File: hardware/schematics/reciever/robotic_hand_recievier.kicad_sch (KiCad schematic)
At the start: 12 parts, among them M1 Motor_Servo, M2 Motor_Servo, M3 Motor_Servo, M4 Motor_Servo, M5 Motor_Servo, U1 XL4016, U2 NRF24L01_Breakout, U3 AMS1117-3.3

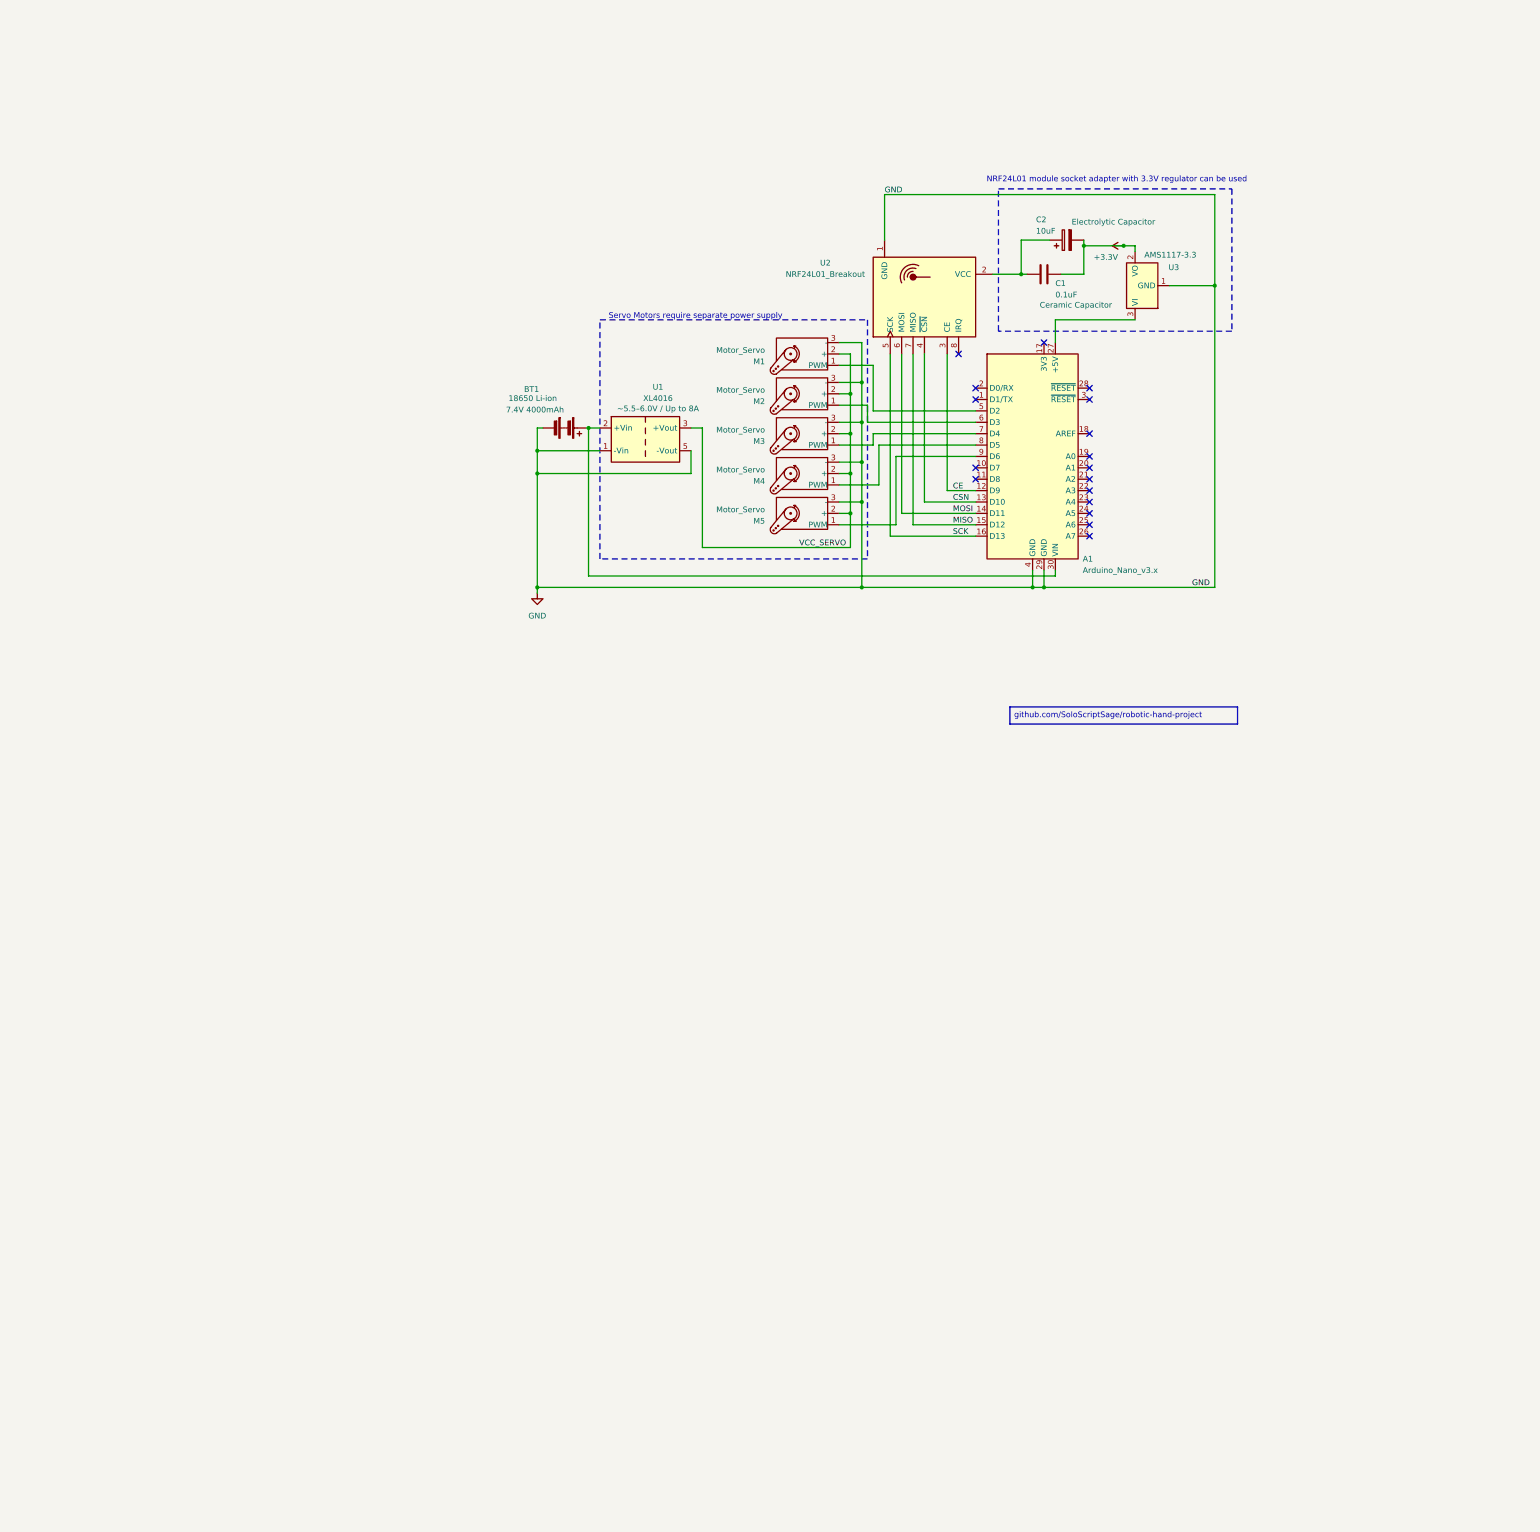
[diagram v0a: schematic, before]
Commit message: Expand schematics and add initial PCB layouts for both boards
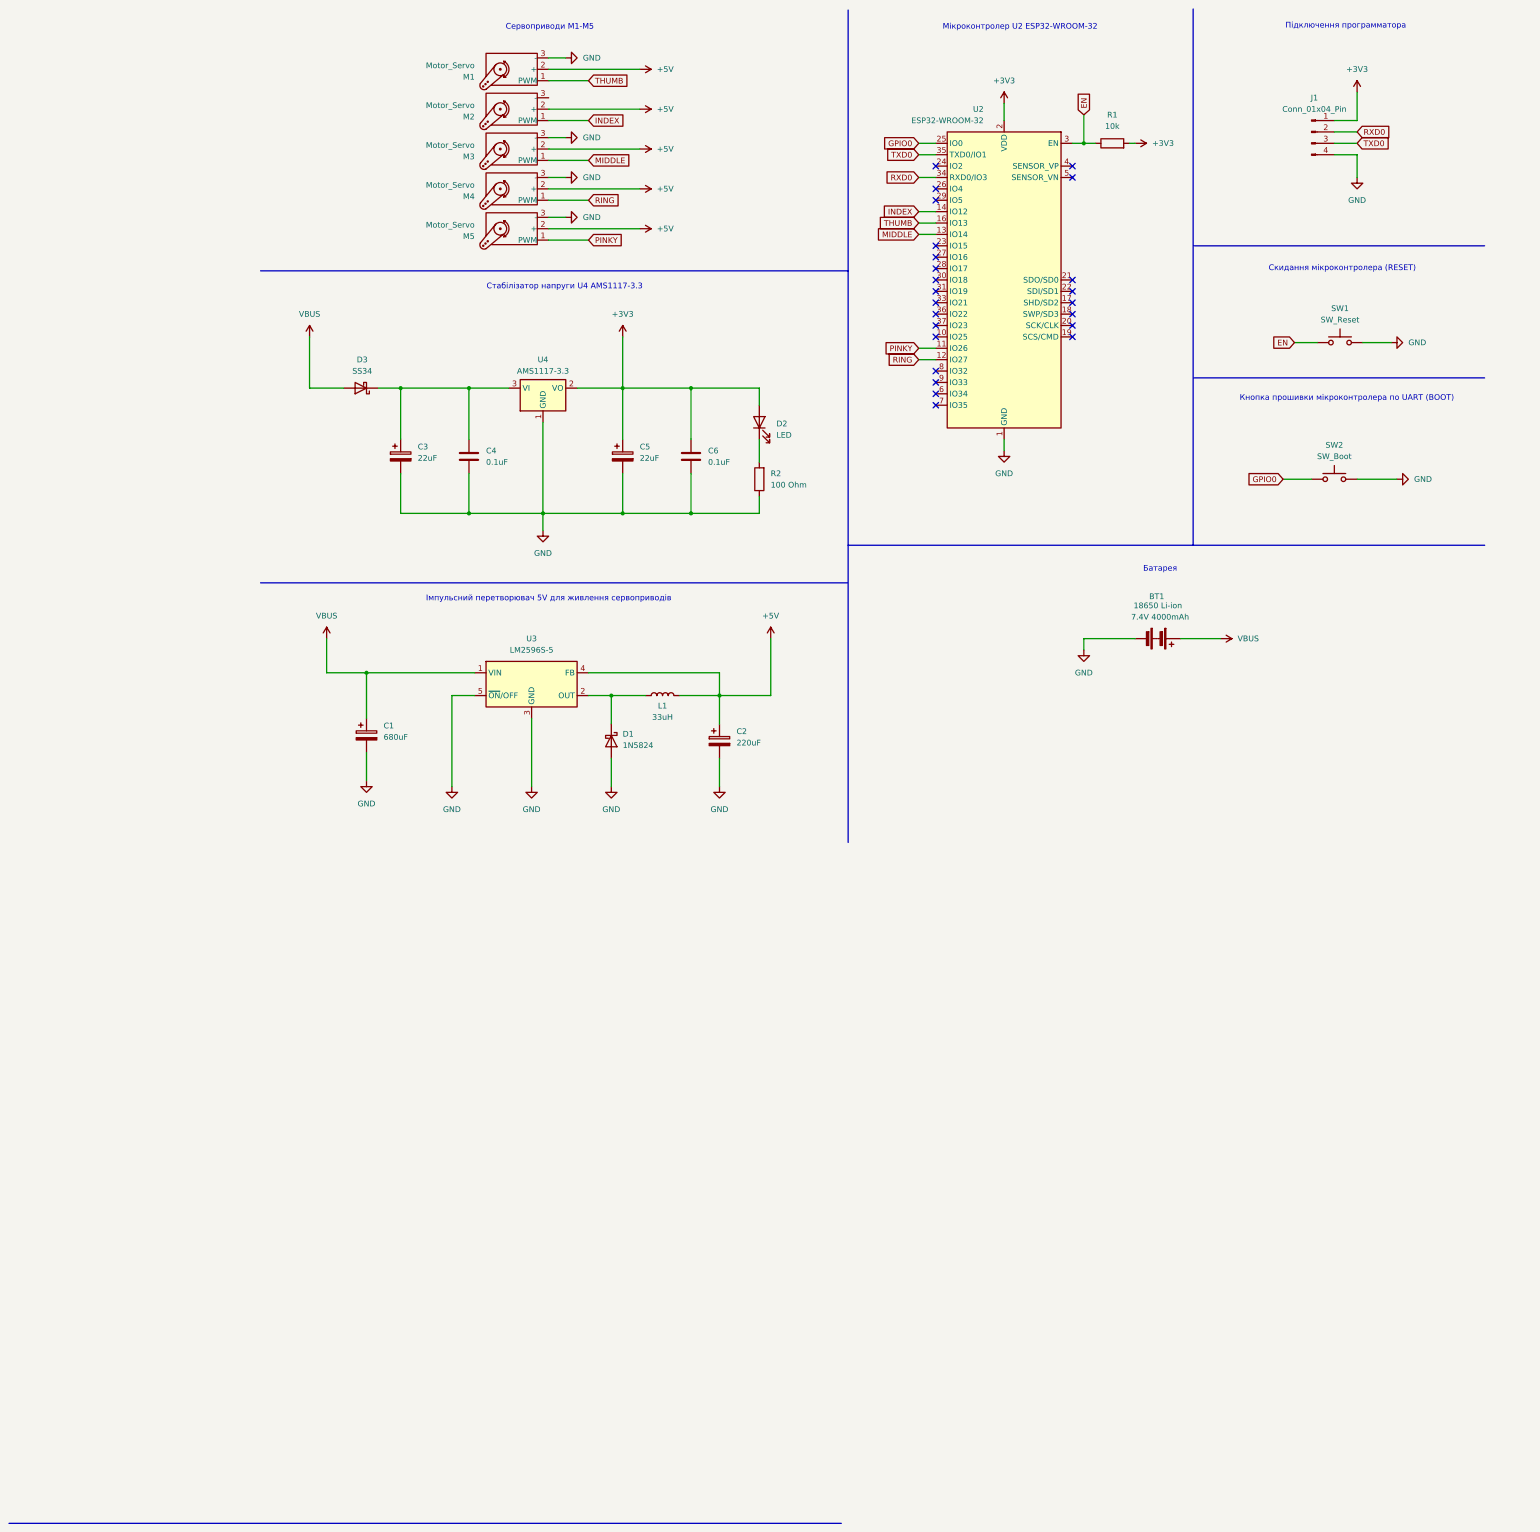
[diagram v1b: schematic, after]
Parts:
- removed A1: Arduino_Nano_v3.x, Module:Arduino_Nano, symbol MCU_Module:Arduino_Nano_v3.x
- removed C1: 0.1uF, symbol Device:C
- removed U1: XL4016, Converter_DCDC:Converter_DCDC_TRACO_TRN3-xx1x_Single_THT, symbol Converter_DCDC:TRN3-2410
- removed U2: NRF24L01_Breakout, RF_Module:nRF24L01_Breakout, symbol RF:NRF24L01_Breakout
- removed U3: AMS1117-3.3, Package_TO_SOT_SMD:SOT-223-3_TabPin2, symbol Regulator_Linear:AMS1117-3.3
- added C1: 680uF, Capacitor_THT:CP_Radial_D8.0mm_P3.50mm, symbol Device:C_Polarized
- added C3, C5: 22uF, Capacitor_SMD:C_1206_3216Metric, symbol Device:C_Polarized
- added C4, C6: 0.1uF, Capacitor_SMD:C_0805_2012Metric, symbol Device:C
- added D1: 1N5824, Diode_SMD:D_SMB, symbol Device:D_Schottky
- added D2: LED, LED_SMD:LED_0805_2012Metric, symbol Device:LED
- added D3: SS34, Diode_SMD:D_SMB, symbol Device:D_Schottky
- added J1: Conn_01x04_Pin, Connector_PinHeader_2.54mm:PinHeader_1x04_P2.54mm_Vertical, symbol Connector:Conn_01x04_Pin
- added L1: 33uH, Inductor_THT:L_Axial_L5.3mm_D2.2mm_P10.16mm_Horizontal_Vishay_IM-1, symbol Device:L
- added R1: 10k, Resistor_SMD:R_0805_2012Metric, symbol Device:R
- added R2: 100 Ohm, Resistor_SMD:R_0805_2012Metric, symbol Device:R
- added SW1: SW_Reset, Button_Switch_SMD:SW_SPST_B3U-1000P, symbol Switch:SW_Push
- added SW2: SW_Boot, Button_Switch_SMD:SW_SPST_B3U-1000P, symbol Switch:SW_Push
- added U2: ESP32-WROOM-32, RF_Module:ESP32-WROOM-32, symbol RF_Module:ESP32-WROOM-32
- added U3: LM2596S-5, Package_TO_SOT_SMD:TO-263-5_TabPin3, symbol Regulator_Switching:LM2596S-5
- added U4: AMS1117-3.3, Package_TO_SOT_SMD:SOT-223-3_TabPin2, symbol Regulator_Linear:AMS1117-3.3
- BT1: footprint (none) -> Robotic Hand:2X-BATTERY-HOLDER-18650
- C2: value 10uF -> 220uF; footprint (none) -> Capacitor_THT:CP_Radial_D8.0mm_P3.50mm; Comment Electrolytic Capacitor -> (none)
- M1, M2, M3, M4, M5: footprint (none) -> Connector_PinHeader_2.54mm:PinHeader_1x03_P2.54mm_Vertical
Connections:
- net +3.3V is gone; now on net GND: C2.2
- net VCC_SERVO is gone; now on net +5V: M1.2 (+), M2.2 (+), M3.2 (+), M4.2 (+), M5.2 (+)
- net GND: now also C1.2, C3.2, C4.2, C5.2, C6.2, D1.2 (A), J1.4 (Pin_4), R2.1, SW1.2, SW2.2, U2.1 (GND), U2.15 (GND), U2.38 (GND), U2.39 (GND), U3.3 (GND), U3.5 (~{ON}/OFF), U4.1 (GND); no longer M2.3 (-)
- net +5V: now reaches C2.1
- net +5V: now also L1.2, U3.4 (FB)
- net VBUS: now reaches BT1.1 (+)
- net VBUS: now also C1.1, D3.2 (A), U3.1 (VIN)
- net THUMB: now reaches M1.1 (PWM)
- net THUMB: now also U2.16 (IO13)
- net INDEX: now reaches M2.1 (PWM)
- net INDEX: now also U2.14 (IO12)
- net MIDDLE: now reaches M3.1 (PWM)
- net MIDDLE: now also U2.13 (IO14)
- net RING: now reaches M4.1 (PWM)
- net RING: now also U2.12 (IO27)
- net PINKY: now reaches M5.1 (PWM)
- net PINKY: now also U2.11 (IO26)
- new net: D1.1 (K), L1.1, U3.2 (OUT)
- new net: D2.1 (K), R2.2
- new net: C3.1, C4.1, D3.1 (K), U4.3 (VI)
- new net +3V3: C5.1, C6.1, D2.2 (A), J1.1 (Pin_1), R1.2, U2.2 (VDD), U4.2 (VO)
- new net EN: R1.1, SW1.1, U2.3 (EN)
- new net GPIO0: SW2.1, U2.25 (IO0)
- new net RXD0: J1.2 (Pin_2), U2.34 (RXD0/IO3)
- new net TXD0: J1.3 (Pin_3), U2.35 (TXD0/IO1)
- no-connect marks 17 -> 24
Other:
- note added: "Імпульсний перетворювач 5V для живлення сервоприводів"
- note added: "Батарея"
- note added: "Кнопка прошивки мікроконтролера по UART (BOOT)"
- note added: "Мікроконтролер U2 ESP32-WROOM-32"
- note added: "Підключення программатора"
- note added: "Сервоприводи M1-M5"
- note added: "Скидання мікроконтролера (RESET)"
- note added: "Стабілізатор напруги U4 AMS1117-3.3"
- note removed: "NRF24L01 module socket adapter with 3.3V regulator can be used"
- note removed: "Servo Motors require separate power supply"
- company: SoloScriptSage -> ХПФК НУ «Львівська політехніка»
- title: Robotic Hand Reciever -> Додаток Б: Схема електрична принципова приймача (RX) 
- moved on the sheet: BT1, M1, M2, M3, M4, M5

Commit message: Revert schematics to rev-A Arduino design; ESP32 redesign split to separate project
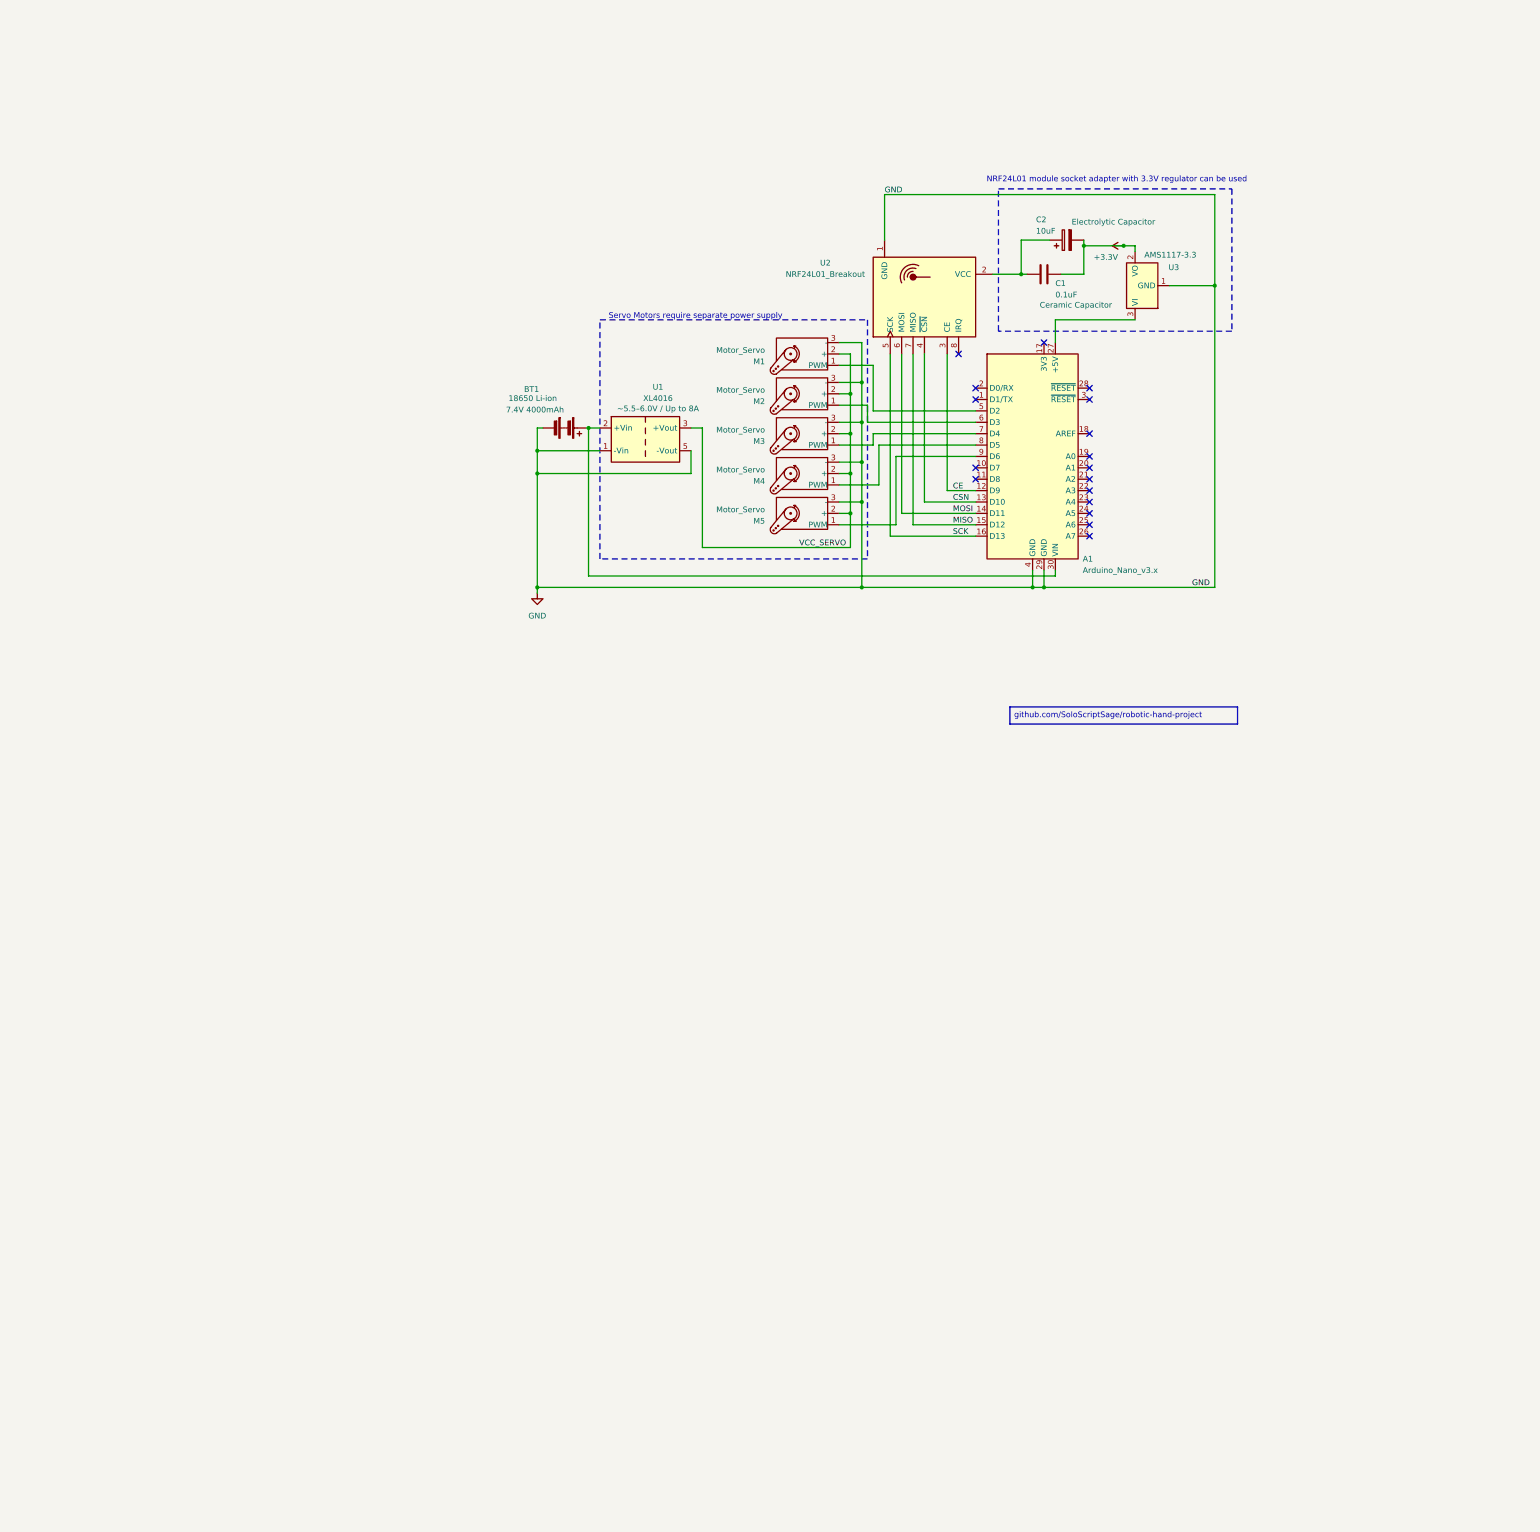
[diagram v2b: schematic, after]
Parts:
- removed C1: 680uF, Capacitor_THT:CP_Radial_D8.0mm_P3.50mm, symbol Device:C_Polarized
- removed C3, C5: 22uF, Capacitor_SMD:C_1206_3216Metric, symbol Device:C_Polarized
- removed C4, C6: 0.1uF, Capacitor_SMD:C_0805_2012Metric, symbol Device:C
- removed D1: 1N5824, Diode_SMD:D_SMB, symbol Device:D_Schottky
- removed D2: LED, LED_SMD:LED_0805_2012Metric, symbol Device:LED
- removed D3: SS34, Diode_SMD:D_SMB, symbol Device:D_Schottky
- removed J1: Conn_01x04_Pin, Connector_PinHeader_2.54mm:PinHeader_1x04_P2.54mm_Vertical, symbol Connector:Conn_01x04_Pin
- removed L1: 33uH, Inductor_THT:L_Axial_L5.3mm_D2.2mm_P10.16mm_Horizontal_Vishay_IM-1, symbol Device:L
- removed R1: 10k, Resistor_SMD:R_0805_2012Metric, symbol Device:R
- removed R2: 100 Ohm, Resistor_SMD:R_0805_2012Metric, symbol Device:R
- removed SW1: SW_Reset, Button_Switch_SMD:SW_SPST_B3U-1000P, symbol Switch:SW_Push
- removed SW2: SW_Boot, Button_Switch_SMD:SW_SPST_B3U-1000P, symbol Switch:SW_Push
- removed U2: ESP32-WROOM-32, RF_Module:ESP32-WROOM-32, symbol RF_Module:ESP32-WROOM-32
- removed U3: LM2596S-5, Package_TO_SOT_SMD:TO-263-5_TabPin3, symbol Regulator_Switching:LM2596S-5
- removed U4: AMS1117-3.3, Package_TO_SOT_SMD:SOT-223-3_TabPin2, symbol Regulator_Linear:AMS1117-3.3
- added A1: Arduino_Nano_v3.x, Module:Arduino_Nano, symbol MCU_Module:Arduino_Nano_v3.x
- added C1: 0.1uF, symbol Device:C
- added U1: XL4016, Converter_DCDC:Converter_DCDC_TRACO_TRN3-xx1x_Single_THT, symbol Converter_DCDC:TRN3-2410
- added U2: NRF24L01_Breakout, RF_Module:nRF24L01_Breakout, symbol RF:NRF24L01_Breakout
- added U3: AMS1117-3.3, Package_TO_SOT_SMD:SOT-223-3_TabPin2, symbol Regulator_Linear:AMS1117-3.3
- BT1: footprint Robotic Hand:2X-BATTERY-HOLDER-18650 -> (none)
- C2: value 220uF -> 10uF; footprint Capacitor_THT:CP_Radial_D8.0mm_P3.50mm -> (none); Comment (none) -> Electrolytic Capacitor
- M1, M2, M3, M4, M5: footprint Connector_PinHeader_2.54mm:PinHeader_1x03_P2.54mm_Vertical -> (none)
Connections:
- net GND: now also M2.3 (-), A1.29 (GND), A1.4 (GND), U1.1 (-Vin), U1.5 (-Vout), U2.1 (GND), U3.1 (GND); no longer C2.2
- net +5V renamed VCC_SERVO
- net VCC_SERVO: now also U1.3 (+Vout); no longer C2.1
- net INDEX: no longer names the net of M2.1 (PWM)
- net INDEX: now also A1.6 (D3)
- net MIDDLE: no longer names the net of M3.1 (PWM)
- net MIDDLE: now also A1.7 (D4)
- net PINKY: no longer names the net of M5.1 (PWM)
- net PINKY: now also A1.9 (D6)
- net RING: no longer names the net of M4.1 (PWM)
- net RING: now also A1.8 (D5)
- net THUMB: no longer names the net of M1.1 (PWM)
- net THUMB: now also A1.5 (D2)
- net VBUS: no longer names the net of BT1.1 (+)
- net VBUS: now also A1.30 (VIN), U1.2 (+Vin)
- new net: C1.1, C2.1, U2.2 (VCC)
- new net: A1.27 (+5V), U3.3 (VI)
- new net +3.3V: C1.2, C2.2, U3.2 (VO)
- new net CE: A1.12 (D9), U2.3 (CE)
- new net CSN: A1.13 (D10), U2.4 (~{CSN})
- new net MISO: A1.15 (D12), U2.7 (MISO)
- new net MOSI: A1.14 (D11), U2.6 (MOSI)
- new net SCK: A1.16 (D13), U2.5 (SCK)
- no-connect marks 24 -> 17
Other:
- note added: "NRF24L01 module socket adapter with 3.3V regulator can be used"
- note added: "Servo Motors require separate power supply"
- note removed: "Імпульсний перетворювач 5V для живлення сервоприводів"
- note removed: "Батарея"
- note removed: "Кнопка прошивки мікроконтролера по UART (BOOT)"
- note removed: "Мікроконтролер U2 ESP32-WROOM-32"
- note removed: "Підключення программатора"
- note removed: "Сервоприводи M1-M5"
- note removed: "Скидання мікроконтролера (RESET)"
- note removed: "Стабілізатор напруги U4 AMS1117-3.3"
- company: ХПФК НУ «Львівська політехніка» -> SoloScriptSage
- title: Додаток Б: Схема електрична принципова приймача (RX)  -> Robotic Hand Reciever
- moved on the sheet: BT1, M1, M2, M3, M4, M5
